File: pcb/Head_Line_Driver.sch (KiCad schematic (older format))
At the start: 8 parts

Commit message: Updates schematic based on some testing. Adds PDF for review
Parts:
- added U? (x2): 74LS04, LED_Chain:SOIC-14, symbol 74xx:74LS04
- added U? (x5): 4071, LED_Chain:SOIC-14, symbol 4xxx:4071
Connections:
- net 3V3: now also U?.14 (VCC), U?.14 (VDD)
- net 5V: now also U?.6 (E3)
- net CASCADE: now also U?.15 (E0), U?.5 (EI); no longer U?.15 (E0)
- net D3: now also U?.1; no longer U?.6 (E3)
- net DIN0: now also U?.11; no longer U?.6 (Q2)
- net DIN1: no longer U?.7 (Q1)
- net DIN2: now also U?.10; no longer U?.9 (Q0)
- net DIN3: now also U?.14 (GS), U?.1; no longer U?.9 (Q0)
- net GND: now also U?.10 (D0), U?.7 (GND), U?.7 (VSS); no longer U?.12 (D2), U?.4 (E1)
- net HD_HORIZ_SHIELD: now also U?.11 (D1); no longer U?.10 (D0)
- net HD_VERT_SHIELD: now also U?.12 (D2); no longer U?.11 (D1)
- net at U?.14 (GS): now also U?.2
- net at U?.6 (Q2): now also U?.9
- net at U?.7 (Q1): now also U?.9
- new net: U?.2, U?.4 (E1)
- new net: U?.13, U?.9 (Q0)
- new net: U?.6 (Q2), U?.8
- new net: U?.7 (Q1), U?.8
- new net: U?.12, U?.9 (Q0)
- new net GS: U?.3
- new net ~E0: U?.15 (E0)
- no-connect marks 10 -> 9
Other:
- note added: "D0 litterally represents null \ni.e. D0 is High, then O0-O2 \nare LOW. \n"
- note added: "The cascaded part is not working.\nAt the moment, the 4071 is not installed."
- moved on the sheet: C?, U?

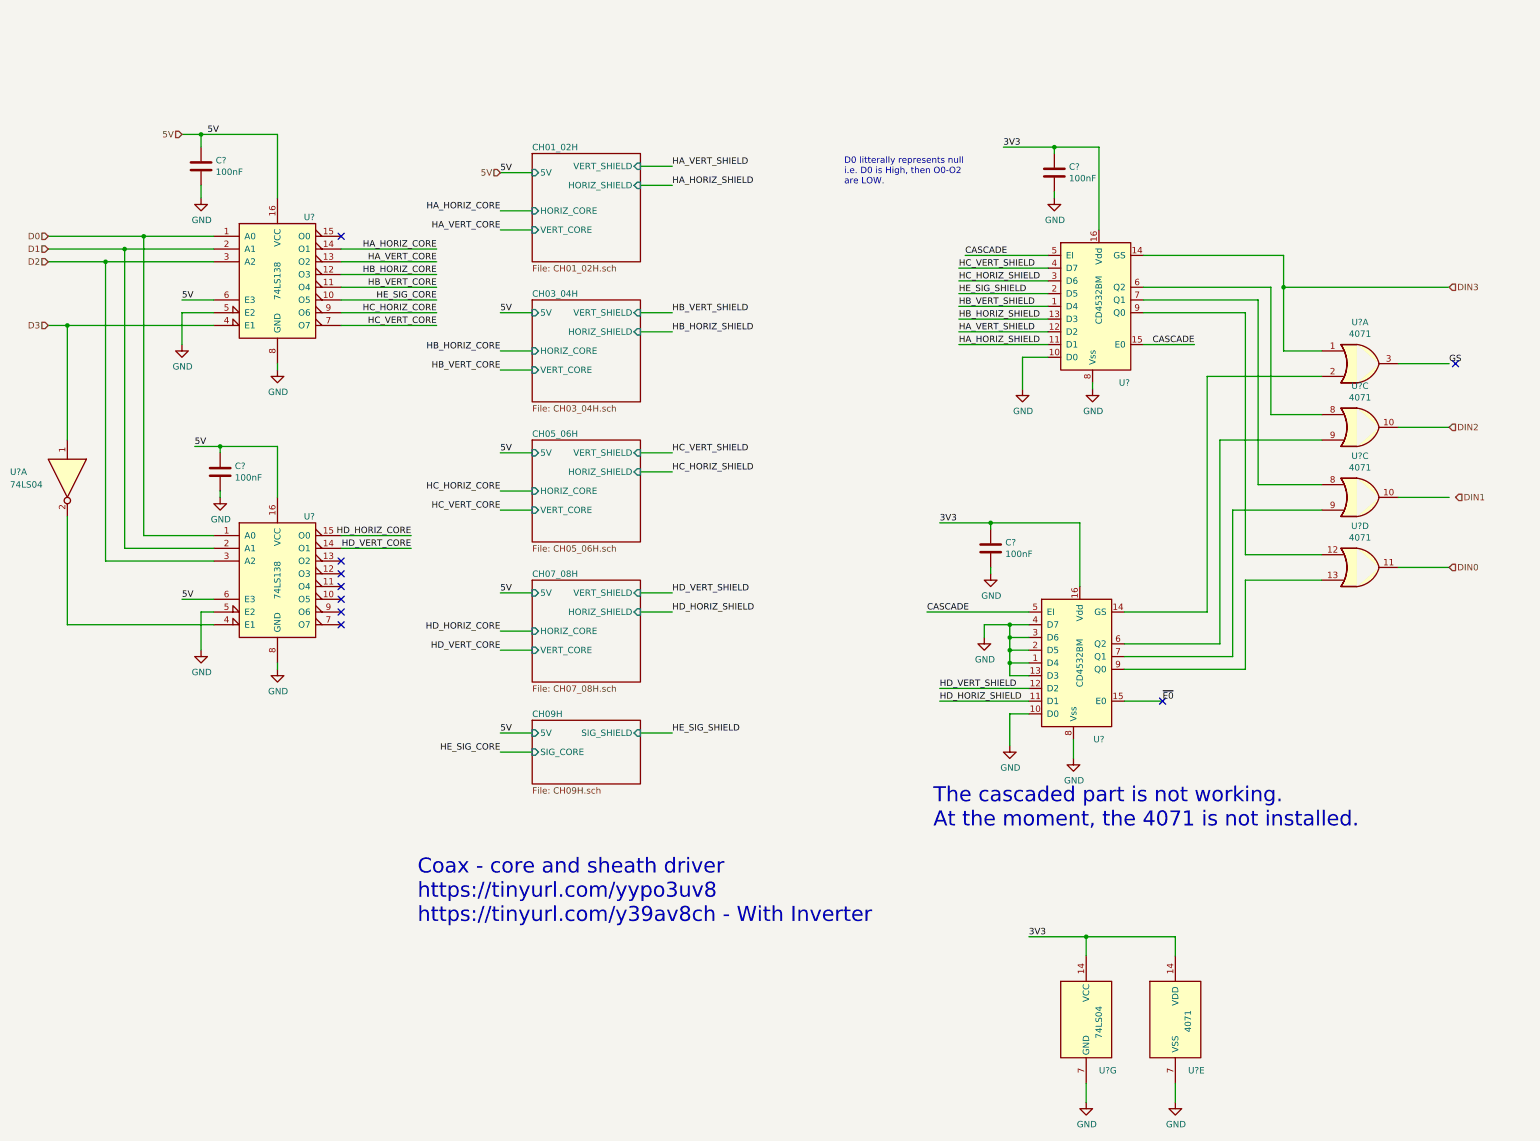
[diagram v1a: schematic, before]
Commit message: Coax driver done - upgrade to kiCad 6
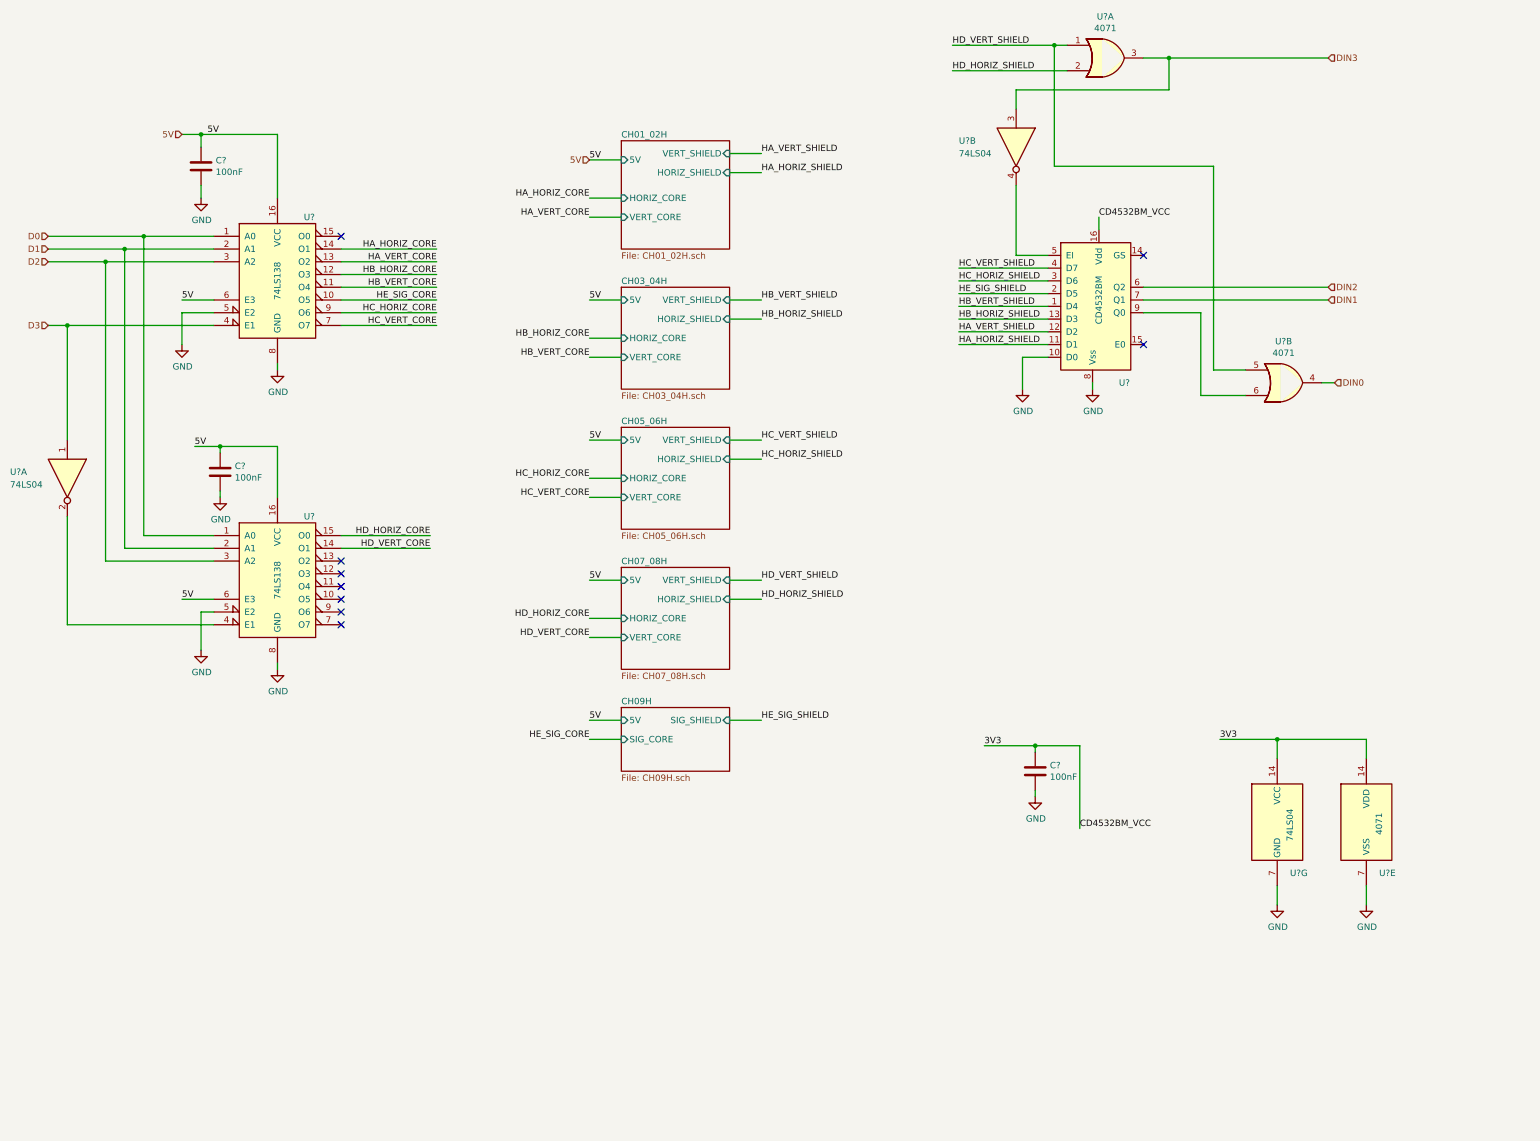
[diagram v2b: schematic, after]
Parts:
- removed C?: 100nF, Capacitor_SMD:C_0805_2012Metric, symbol Device:C
- removed U?: CD4532BM, Package_SO:SO-16_3.9x9.9mm_P1.27mm, symbol CoaxTester:CD4532BM
- removed U? (x2): 4071, LED_Chain:SOIC-14, symbol 4xxx:4071
- added U?: 74LS04, LED_Chain:SOIC-14, symbol 74xx:74LS04
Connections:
- net GS is gone; now on net DIN3: U?.3
- net DIN0: now also U?.4
- net DIN1: now also U?.7 (Q1)
- net DIN2: now also U?.6 (Q2); no longer U?.10
- net DIN3: now also U?.3; no longer U?.1, U?.14 (GS)
- net HD_HORIZ_SHIELD: now also U?.2
- net HD_VERT_SHIELD: now also U?.1, U?.5
- net at U?.9 (Q0): now also U?.6
- net CASCADE: no longer names the net of U?.15 (E0)
- net CASCADE: no longer U?.5 (EI)
- new net: U?.4, U?.5 (EI)
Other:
- note removed: "Coax - core and sheath driver\nhttps://tinyurl.com/yypo3uv8\nhttps://tinyurl.com/y39av8ch - With Inverter"
- note removed: "D0 litterally represents null \ni.e. D0 is High, then O0-O2 \nare LOW. \n"
- note removed: "The cascaded part is not working.\nAt the moment, the 4071 is not installed."
- moved on the sheet: C?, U?A, U?E, U?G
